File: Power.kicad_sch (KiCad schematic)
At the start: 30 parts, among them J201 Screw_Terminal_01x02_P5mm, J202 USB-C_304A-ACP16X, U201 TPS5430DDA, U202 NUCLEO64-H503RB

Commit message: Continued to check components footprints
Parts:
- F201: Checked To check value -> E - To check value
- J202: Checked (none) -> OK
- R202: Checked 1K8?? -> E- 1K8??
- U201: Checked Footprint -> E- Footprint
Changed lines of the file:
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@@
 			)
 		)
-		(property "Checked" "1K8??"
+		(property "Checked" "E- 1K8??"
 			(at 191.77 48.26 0)
 			(effects
@@
 			)
 		)
-		(property "Checked" "Footprint"
+		(property "Checked" "E- Footprint"
 			(at 147.32 38.1 0)
 			(effects
@@
 			)
 		)
-		(property "Checked" ""
+		(property "Checked" "OK"
 			(at 33.02 158.75 0)
 			(effects
@@
 			)
 		)
-		(property "Checked" "To check value"
+		(property "Checked" "E - To check value"
 			(at 58.42 144.78 90)
 			(effects

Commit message: Changed two connectors
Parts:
- U202: footprint ProjectConnectors:Nucleo64 -> ProjectConnectors:Nucleo64_ST-Morpho
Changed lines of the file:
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@@
 			)
 		)
-		(property "Footprint" "ProjectConnectors:Nucleo64"
+		(property "Footprint" "ProjectConnectors:Nucleo64_ST-Morpho"
 			(at 177.292 140.208 0)
 			(effects

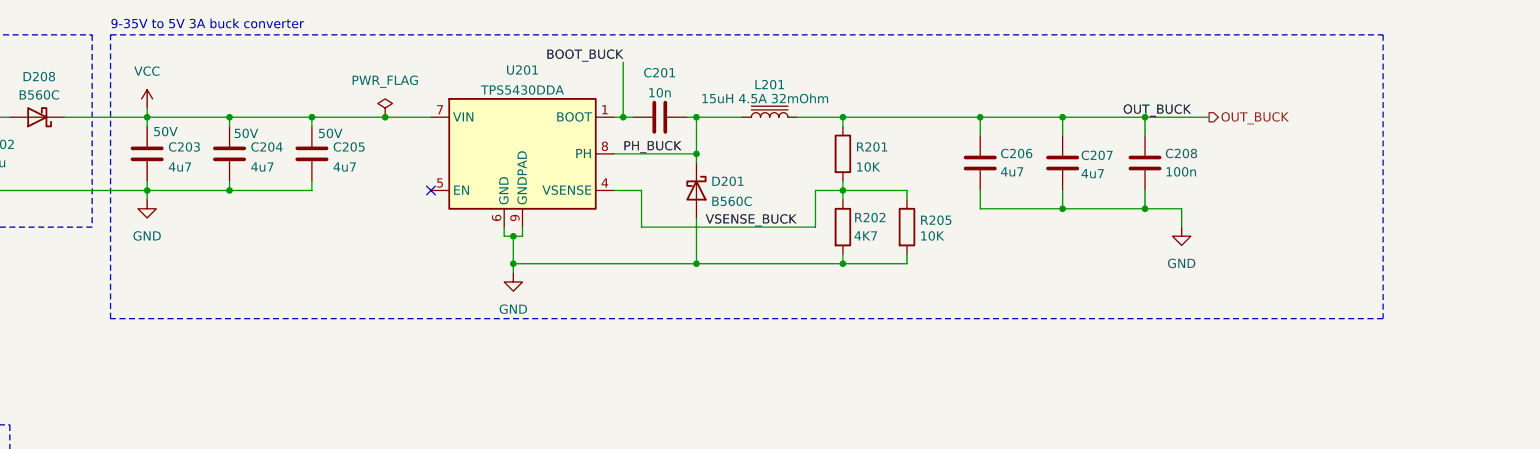
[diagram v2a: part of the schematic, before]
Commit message: Started the floorplan + added the Power LED
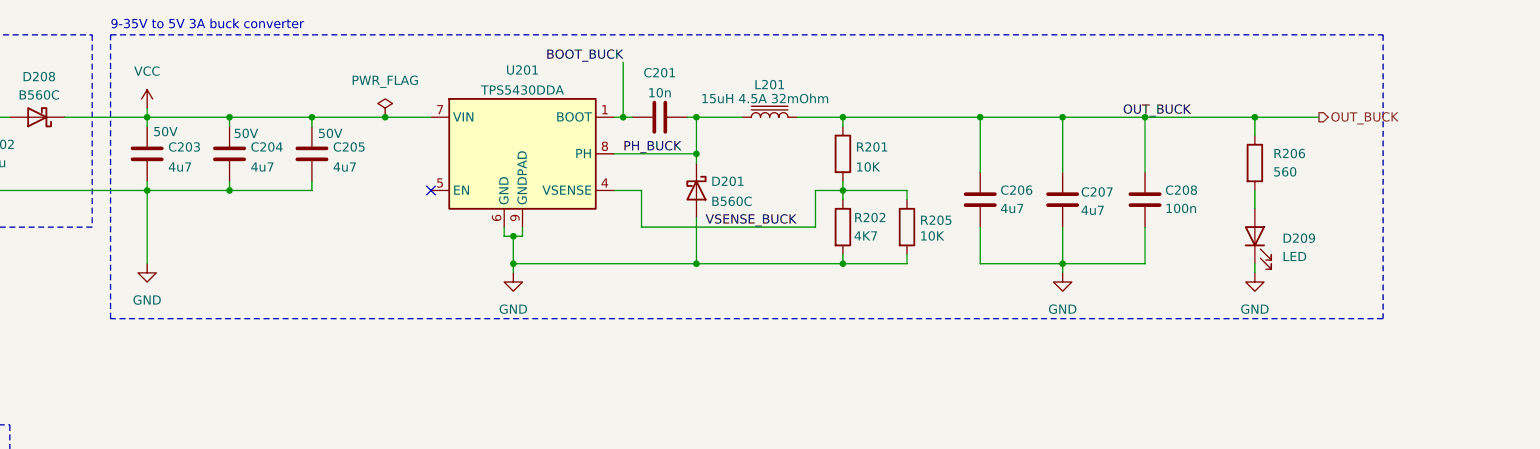
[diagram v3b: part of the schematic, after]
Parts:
- added D209: LED, LED_SMD:LED_0603_1608Metric, symbol Device:LED
- added R206: 560, Resistor_SMD:R_0603_1608Metric_Pad0.98x0.95mm_HandSolder, symbol Device:R
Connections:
- net GND: now also D209.1 (K)
- net OUT_BUCK: now also R206.1
- new net: D209.2 (A), R206.2
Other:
- moved on the sheet: C206, C207, C208

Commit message: some placement
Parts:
- D201, D208: value B560C -> B340A-13-F; footprint Diode_SMD:D_SMB-SMC_Universal_Handsoldering -> Diode_SMD:D_SMA; LCSC C85100 -> C85098
- L201: value 15uH 4.5A 32mOhm -> SLO0630H150MTT; footprint Inductor_SMD:L_12x12mm_H8mm -> Inductor_SMD:L_AVX_LMLP07A7; LCSC C40000 -> C182182
- R202: value 4K7 -> 4K3; Checked E- 1K8?? -> OK; LCSC C4177 -> C23159
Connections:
- net D+: no longer names the net of J202.6 (DP1)
- net D+: no longer J202.8 (DP2)
- net D-: no longer names the net of J202.5 (DN2)
- net D-: no longer J202.7 (DN1)
- no-connect marks 4 -> 8
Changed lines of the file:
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@@
 	(rectangle
 		(start 90.17 21.59)
-		(end 266.7 60.96)
+		(end 270.51 60.96)
 		(stroke
 			(width 0)
@@
 	)
 	(junction
-		(at 46.99 158.75)
-		(diameter 0)
-		(color 0 0 0 0)
-	)
-	(junction
 		(at 50.8 85.09)
 		(diameter 0)
@@
 	)
 	(junction
-		(at 46.99 165.1)
-		(diameter 0)
-		(color 0 0 0 0)
-	)
-	(junction
 		(at 161.29 33.02)
 		(diameter 0)
@@
 	)
 	(no_connect
+		(at 45.72 161.29)
+	)
+	(no_connect
 		(at 219.71 123.19)
 	)
 	(no_connect
+		(at 45.72 165.1)
+	)
+	(no_connect
+		(at 45.72 158.75)
+	)
+	(no_connect
 		(at 45.72 172.72)
 	)
@@
 		(at 45.72 175.26)
 	)
+	(no_connect
+		(at 45.72 167.64)
+	)
 	(wire
 		(pts
@@
 	(wire
 		(pts
-			(xy 45.72 158.75) (xy 46.99 158.75)
-		)
-		(stroke
-			(width 0)
-			(type default)
-		)
-	)
-	(wire
-		(pts
 			(xy 69.85 144.78) (xy 74.93 144.78)
 		)
@@
 	(wire
 		(pts
-			(xy 46.99 167.64) (xy 46.99 165.1)
-		)
-		(stroke
-			(width 0)
-			(type default)
-		)
-	)
-	(wire
-		(pts
 			(xy 200.66 128.27) (xy 187.96 128.27)
 		)
@@
 	(wire
 		(pts
-			(xy 46.99 165.1) (xy 50.8 165.1)
-		)
-		(stroke
-			(width 0)
-			(type default)
-		)
-	)
-	(wire
-		(pts
 			(xy 191.77 41.91) (xy 191.77 43.18)
 		)
@@
 	(wire
 		(pts
-			(xy 45.72 161.29) (xy 46.99 161.29)
-		)
-		(stroke
-			(width 0)
-			(type default)
-		)
-	)
-	(wire
-		(pts
 			(xy 106.68 43.18) (xy 118.11 43.18)
 		)
@@
 	(wire
 		(pts
-			(xy 45.72 165.1) (xy 46.99 165.1)
-		)
-		(stroke
-			(width 0)
-			(type default)
-		)
-	)
-	(wire
-		(pts
 			(xy 187.96 153.67) (xy 200.66 153.67)
 		)
@@
 	(wire
 		(pts
-			(xy 45.72 167.64) (xy 46.99 167.64)
-		)
-		(stroke
-			(width 0)
-			(type default)
-		)
-	)
-	(wire
-		(pts
-			(xy 46.99 158.75) (xy 50.8 158.75)
-		)
-		(stroke
-			(width 0)
-			(type default)
-		)
-	)
-	(wire
-		(pts
 			(xy 161.29 25.4) (xy 161.29 33.02)
 		)
@@
 	(wire
 		(pts
-			(xy 46.99 161.29) (xy 46.99 158.75)
-		)
-		(stroke
-			(width 0)
-			(type default)
-		)
-	)
-	(wire
-		(pts
 			(xy 210.82 33.02) (xy 222.25 33.02)
 		)
@@
 		)
 	)
-	(label "D+"
-		(at 50.8 158.75 180)
-		(effects
-			(font
-				(size 1.27 1.27)
-			)
-			(justify right bottom)
-		)
-	)
-	(label "D-"
-		(at 50.8 165.1 180)
-		(effects
-			(font
-				(size 1.27 1.27)
-			)
-			(justify right bottom)
-		)
-	)
 	(label "OUT_BUCK"
 		(at 240.03 33.02 180)
@@
 			)
 		)
-		(property "Value" "4K7"
+		(property "Value" "4K3"
 			(at 193.294 49.53 0)
 			(effects
@@
 			)
 		)
-		(property "LCSC" "C4177"
+		(property "LCSC" "C23159"
 			(at 191.77 48.26 0)
 			(effects
@@
 			)
 		)
-		(property "Checked" "E- 1K8??"
+		(property "Checked" "OK"
 			(at 191.77 48.26 0)
 			(effects
@@
 	)
 	(symbol
+		(lib_id "Device:D_Schottky")
+		(at 80.01 33.02 180)
+		(unit 1)
+		(exclude_from_sim no)
+		(in_bom yes)
+		(on_board yes)
+		(dnp no)
+		(fields_autoplaced yes)
+		(property "Reference" "D208"
+			(at 80.3275 26.67 0)
+			(effects
+				(font
+					(size 1.27 1.27)
+				)
+			)
+		)
+		(property "Value" "B340A-13-F"
+			(at 80.3275 29.21 0)
+			(effects
+				(font
+					(size 1.27 1.27)
+				)
+			)
+		)
+		(property "Footprint" "Diode_SMD:D_SMA"
+			(at 80.01 33.02 0)
+			(effects
+				(font
+					(size 1.27 1.27)
+				)
+				(hide yes)
+			)
+		)
+		(property "Datasheet" "https://www.lcsc.com/datasheet/C85098.pdf?spm=wm.sxq.inf.ggs___wm.fly.bg.0.xh&lcsc_vid=ElYPBF1VFFcMAwEFElVaVlEHRVFdU1VeTwBYVFJTElUxVlNRQFJeVldeQFhfUTsOAxUeFF5JWBYZEEoKFBINSQcJGk4%3D"
+			(at 80.01 33.02 0)
+			(effects
+				(font
+					(size 1.27 1.27)
+				)
+				(hide yes)
+			)
+		)
+		(property "Description" ""
+			(at 80.01 33.02 0)
+			(effects
+				(font
+					(size 1.27 1.27)
+				)
+			)
+		)
+		(property "LCSC" "C85098"
+			(at 80.01 33.02 90)
+			(effects
+				(font
+					(size 1.27 1.27)
+				)
+				(hide yes)
+			)
+		)
+		(property "Sim.Type" ""
+			(at 80.01 33.02 90)
+			(effects
+				(font
+					(size 1.27 1.27)
+				)
+				(hide yes)
+			)
+		)
+		(property "Checked" "OK"
+			(at 80.01 33.02 90)
+			(effects
+				(font
+					(size 1.27 1.27)
+				)
+				(hide yes)
+			)
+		)
+		(pin "1"
+		)
+		(pin "2"
+		)
+		(instances
+			(project "Educational-Board_MainBoard"
+				(path "/835b4df9-7d62-45f4-81d2-5a64fbc86f3c/a1b70c1b-93fd-432d-b3bf-990581065c7c"
+					(reference "D208")
+					(unit 1)
+				)
+			)
+		)
+	)
+	(symbol
 		(lib_id "Device:L_Iron")
 		(at 181.61 33.02 90)
@@
 		(dnp no)
 		(property "Reference" "L201"
-			(at 181.61 28.5455 90)
+			(at 181.61 27.686 90)
 			(effects
 				(font
@@
 			)
 		)
-		(property "Value" "15uH 4.5A 32mOhm"
+		(property "Value" "SLO0630H150MTT"
 			(at 180.975 30.48 90)
 			(effects
@@
 			)
 		)
-		(property "Footprint" "Inductor_SMD:L_12x12mm_H8mm"
+		(property "Footprint" "Inductor_SMD:L_AVX_LMLP07A7"
 			(at 181.61 33.02 0)
 			(effects
@@
 			)
 		)
-		(property "Datasheet" "https://www.lcsc.com/datasheet/C40000.pdf"
+		(property "Datasheet" "https://www.lcsc.com/datasheet/C182182.pdf?spm=wm.sxq.inf.ggs___wm.fly.bg.0.xh&lcsc_vid=ElYPBF1VFFcMAwEFElVaVlEHRVFdU1VeTwBYVFJTElUxVlNRQFJeVldeQFhfUTsOAxUeFF5JWBYZEEoKFBINSQcJGk4%3D"
 			(at 181.61 33.02 0)
 			(effects
@@
 			)
 		)
-		(property "LCSC" "C40000"
+		(property "LCSC" "C182182"
 			(at 181.61 33.02 90)
 			(effects
@@
 			)
 		)
-		(property "Value" "B560C"
+		(property "Value" "B340A-13-F"
 			(at 173.482 44.7291 90)
 			(effects
@@
 			)
 		)
-		(property "Footprint" "Diode_SMD:D_SMB-SMC_Universal_Handsoldering"
+		(property "Footprint" "Diode_SMD:D_SMA"
 			(at 171.45 43.18 0)
 			(effects
@@
 			)
 		)
-		(property "Datasheet" "https://www.lcsc.com/datasheet/C85100.pdf"
+		(property "Datasheet" "https://www.lcsc.com/datasheet/C85098.pdf?spm=wm.sxq.inf.ggs___wm.fly.bg.0.xh&lcsc_vid=ElYPBF1VFFcMAwEFElVaVlEHRVFdU1VeTwBYVFJTElUxVlNRQFJeVldeQFhfUTsOAxUeFF5JWBYZEEoKFBINSQcJGk4%3D"
 			(at 171.45 43.18 0)
 			(effects
@@
 			)
 		)
-		(property "LCSC" "C85100"
+		(property "LCSC" "C85098"
 			(at 171.45 43.18 90)
 			(effects
@@
 					(unit 1)
 				)
-			)
-		)
-	)
-	(symbol
-		(lib_id "Device:D_Schottky")
-		(at 80.01 33.02 180)
-		(unit 1)
-		(exclude_from_sim no)
-		(in_bom yes)
-		(on_board yes)
-		(dnp no)
-		(property "Reference" "D208"
-			(at 80.264 27.432 0)
-			(effects
-				(font
-					(size 1.27 1.27)
-				)
-			)
-		)
-		(property "Value" "B560C"
-			(at 80.264 29.972 0)
-			(effects
-				(font
-					(size 1.27 1.27)
-				)
-			)
-		)
-		(property "Footprint" "Diode_SMD:D_SMB-SMC_Universal_Handsoldering"
-			(at 80.01 33.02 0)
-			(effects
-				(font
-					(size 1.27 1.27)
-				)
-				(hide yes)
-			)
-		)
-		(property "Datasheet" "https://www.lcsc.com/datasheet/C85100.pdf"
-			(at 80.01 33.02 0)
-			(effects
-				(font
-					(size 1.27 1.27)
-				)
-				(hide yes)
-			)
-		)
-		(property "Description" ""
-			(at 80.01 33.02 0)
-			(effects
-				(font
-					(size 1.27 1.27)
-				)
-			)
-		)
-		(property "LCSC" "C85100"
-			(at 80.01 33.02 90)
-			(effects
-				(font
-					(size 1.27 1.27)
-				)
-				(hide yes)
-			)
-		)
-		(property "Sim.Type" ""
-			(at 80.01 33.02 0)
-			(effects
-				(font
-					(size 1.27 1.27)
-				)
-				(hide yes)
-			)
-		)
-		(property "Checked" "OK"
-			(at 80.01 33.02 0)
-			(effects
-				(font
-					(size 1.27 1.27)
-				)
-				(hide yes)
-			)
-		)
-		(pin "1"
-		)
-		(pin "2"
-		)
-		(instances
-			(project "Educational-Board_MainBoard"
-				(path "/835b4df9-7d62-45f4-81d2-5a64fbc86f3c/a1b70c1b-93fd-432d-b3bf-990581065c7c"
-					(reference "D208")
-					(unit 1)
-				)

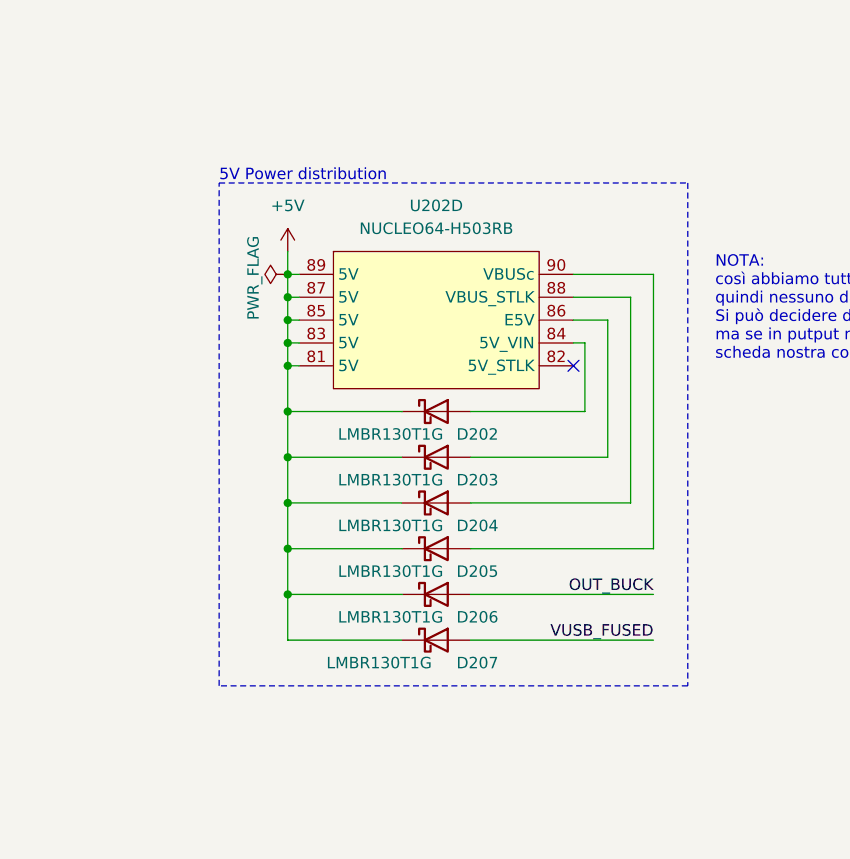
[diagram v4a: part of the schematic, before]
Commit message: Added some netclasses + started routing of some small parts + reordered some groups
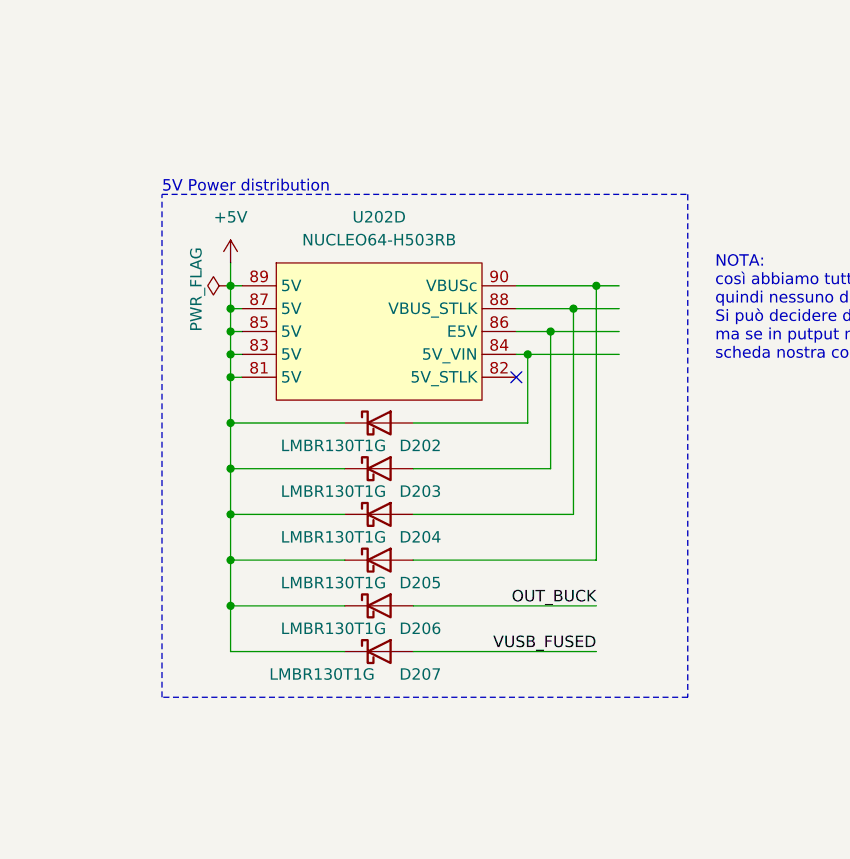
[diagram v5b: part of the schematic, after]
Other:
- moved on the sheet: D202, D203, D204, D205, D206, D207, U202D

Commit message: routing and silkscreen logo
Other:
- company: Filippo Castellan, Alan Masutti -> Alan Masutti, Filippo Castellan
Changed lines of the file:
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@@
 		(date "2026-03-12")
 		(rev "1.0")
-		(company "Filippo Castellan, Alan Masutti")
+		(company "Alan Masutti, Filippo Castellan")
 	)
 	(rectangle

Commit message: added version marking, generated all the production files, added last connector lcsc number
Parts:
- U202: now not fitted
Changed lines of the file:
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@@
 		(in_bom no)
 		(on_board yes)
-		(dnp no)
+		(dnp yes)
 		(fields_autoplaced yes)
 		(property "Reference" "U202"
